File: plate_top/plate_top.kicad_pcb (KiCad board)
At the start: 2 copper layers, 177.4 x 117.9 mm, 32 parts, among them SW1 SW_Push, SW10 SW_Push, SW11 SW_Push, SW12 SW_Push, SW13 SW_Push, SW14 SW_Push, SW15 SW_Push, SW16 SW_Push, SW17 SW_Push, SW18 SW_Push, SW19 SW_Push, SW2 SW_Push, SW20 SW_Push, SW21 SW_Push, SW22 SW_Push, SW23 SW_Push, SW24 SW_Push, SW25 SW_Push, SW26 SW_Push, SW27 SW_Push, SW28 SW_Push, SW29 SW_Push, SW3 SW_Push, SW30 SW_Push, SW31 SW_Push, SW32 SW_Push, SW4 SW_Push, SW5 SW_Push, SW6 SW_Push, SW7 SW_Push, SW8 SW_Push, SW9 SW_Push

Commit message: Plates
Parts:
- added H16: MountingHole, used_footprints:M2_HOLE_PCB, F.Cu at (203.0, 86.6)
- added HM1: CaseHole, used_footprints:M2_HOLE_PCB, F.Cu at (214.5, 114.9)
- added HM10: CaseHole, used_footprints:M2_HOLE_PCB, F.Cu at (171.8, 74.4)
- added HM11: CaseHole, used_footprints:M2_HOLE_PCB, F.Cu at (135.9, 60.3)
- added HM13: CaseHole, used_footprints:M2_HOLE_PCB, F.Cu at (133.3, 105.5)
- added HM14: CaseHole, used_footprints:M2_HOLE_PCB, F.Cu at (176.3, 120.2)
- added HM2: CaseHole, used_footprints:M2_HOLE_PCB, F.Cu at (176.5, 55.3)
- added HM3: CaseHole, used_footprints:M2_HOLE_PCB, F.Cu at (194.2, 134.6)
- added HM4: CaseHole, used_footprints:M2_HOLE_PCB, F.Cu at (155.5, 110.3)
- added HM5: CaseHole, used_footprints:M2_HOLE_PCB, F.Cu at (72.8, 75.9)
- added HM6: CaseHole, used_footprints:M2_HOLE_PCB, F.Cu at (91.4, 80.9)
- added HM7: CaseHole, used_footprints:M2_HOLE_PCB, F.Cu at (96.5, 42.5)
- added HM8: CaseHole, used_footprints:M2_HOLE_PCB, F.Cu at (93.9, 62.0)
- added HM9: CaseHole, used_footprints:M2_HOLE_PCB, F.Cu at (138.5, 44.8)
- moved SW19 51.5 mm to (210.6, 136.5), turned to 127.5 degrees
- moved SW32 33.8 mm to (195.5, 148.1), turned to 307.5 degrees
- moved SW27 30.7 mm to (64.0, 70.0), turned to 172.5 degrees
- moved SW20 30.6 mm to (80.7, 89.1), turned to 172.5 degrees
- moved SW26 30.4 mm to (192.7, 118.2), turned to 141 degrees
- moved SW28 28.6 mm to (122.0, 112.7), turned to 0 degrees
- moved SW21 28.4 mm to (99.6, 91.5), turned to 172.5 degrees
- moved SW31 27.7 mm to (180.8, 133.0), turned to 321 degrees
- moved SW13 27.5 mm to (83.2, 70.2), turned to 172.5 degrees
- moved SW22 25.7 mm to (119.8, 90.2), turned to 168 degrees
- moved SW25 25.1 mm to (175.2, 104.3), turned to 168 degrees
- moved SW14 25.0 mm to (102.1, 72.7), turned to 172.5 degrees
- moved SW7 24.7 mm to (85.7, 51.3), turned to 172.5 degrees
- moved SW29 24.5 mm to (142.8, 114.9), turned to 348 degrees
- moved SW24 24.3 mm to (157.1, 98.1), turned to 168 degrees
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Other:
- board size 177.4 x 117.9 mm -> 170.3 x 138.9 mm

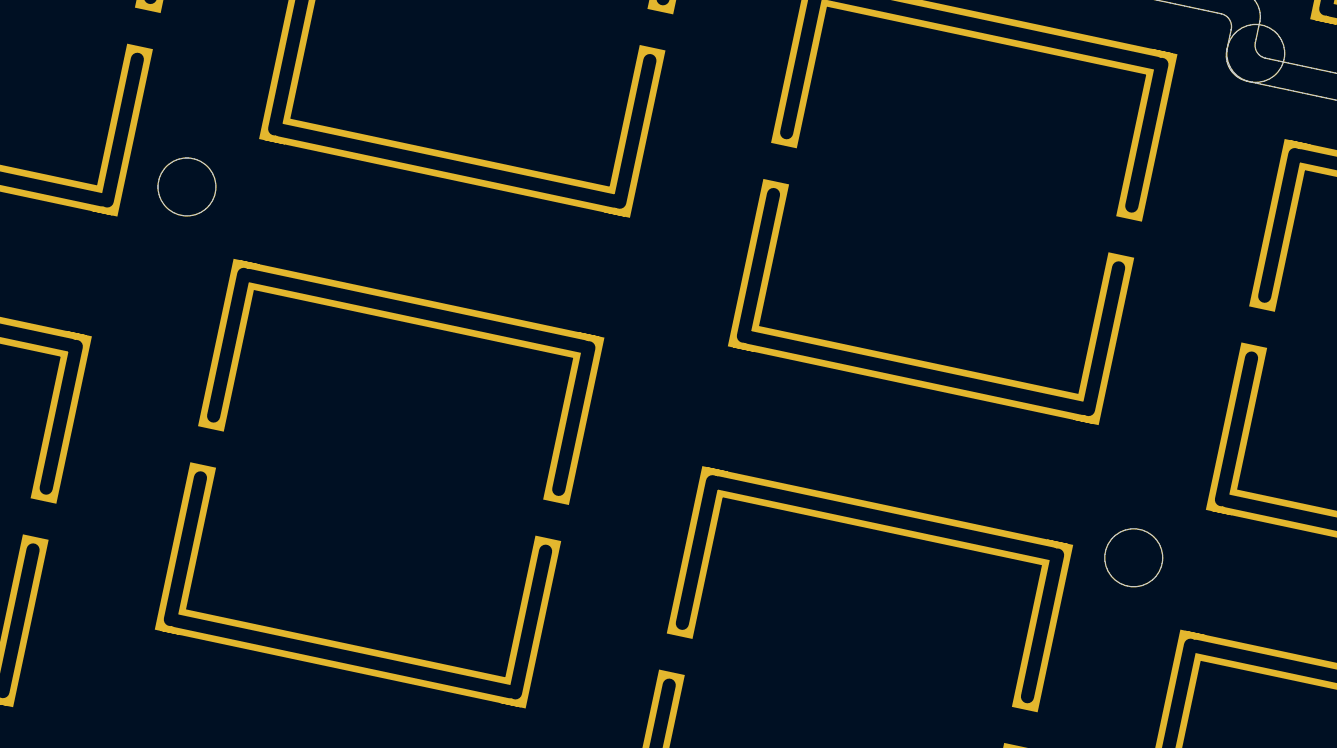
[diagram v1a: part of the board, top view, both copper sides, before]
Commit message: Moved two mounting holes a bit
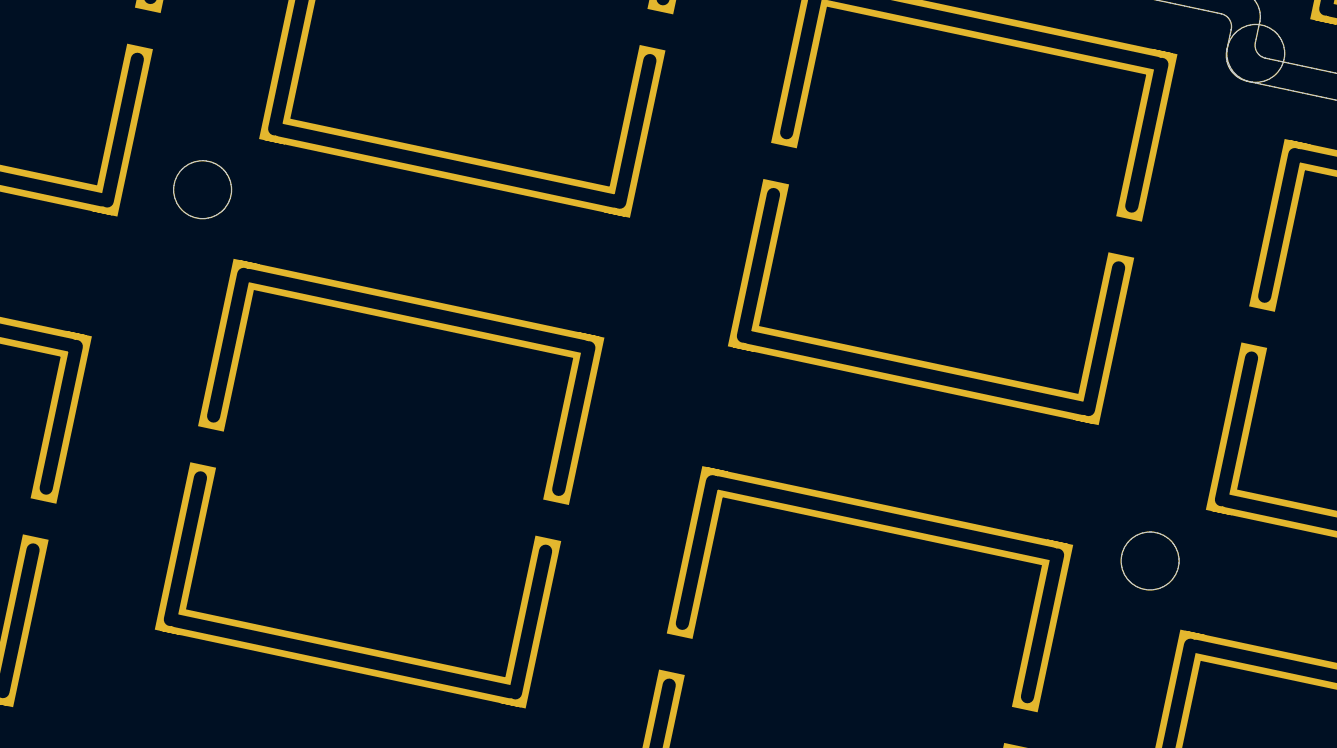
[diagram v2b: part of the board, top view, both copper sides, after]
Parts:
- moved HM10 0.63 mm to (172.5, 74.5)
- moved HM11 0.60 mm to (136.5, 60.4)

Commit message: WIP
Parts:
- moved H16 9.35 mm to (200.2, 95.6)
- moved SW13 9.21 mm to (81.0, 79.1)
- moved SW17 9.21 mm to (158.8, 88.4)
- moved SW20 9.21 mm to (78.5, 98.0)
- moved SW21 9.21 mm to (97.4, 100.5)
- moved SW27 9.21 mm to (61.8, 78.9)
- moved HM14 9.21 mm to (174.1, 129.1)
- moved HM2 9.21 mm to (174.3, 64.2)
- moved HM9 9.21 mm to (136.3, 53.8)
- moved SW10 9.21 mm to (145.0, 61.9)
- moved SW24 9.21 mm to (154.8, 107.0)
- moved SW6 9.21 mm to (184.9, 57.3)
- moved SW7 9.21 mm to (83.5, 60.2)
- moved HM1 9.21 mm to (212.3, 123.8)
- moved HM11 9.21 mm to (134.3, 69.4)
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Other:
- board size 170.3 x 138.9 mm -> 173.5 x 138.9 mm

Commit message: Multiple fixes
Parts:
- moved HM1 12.4 mm to (222.7, 117.2)
- moved HM10 10.9 mm to (172.1, 72.7)
- moved HM11 10.9 mm to (136.2, 58.6)
- moved SW27 10.9 mm to (63.7, 68.2)
- moved HM9 10.9 mm to (138.2, 43.0)
- moved HM8 10.9 mm to (93.6, 60.2)
- moved SW30 10.9 mm to (162.5, 119.9)
- moved SW5 10.9 mm to (168.6, 40.4)
- moved HM2 10.9 mm to (176.2, 53.5)
- moved SW29 10.9 mm to (142.5, 113.1)
- moved SW7 10.9 mm to (85.4, 49.5)
- moved SW24 10.9 mm to (156.7, 96.3)
- moved SW1 10.9 mm to (87.9, 30.6)
- moved SW20 10.9 mm to (80.4, 87.3)
- moved SW14 10.9 mm to (101.8, 70.9)
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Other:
- outline, holes or cut-outs redrawn

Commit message: Holes and top plate
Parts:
- removed H16: MountingHole, used_footprints:M2_HOLE_PCB
- removed HM1: CaseHole, used_footprints:M2_HOLE_PCB
- SW1, SW10, SW11, SW12, SW13, SW14, SW15, SW16, SW17, SW18, SW19, SW2, SW20, SW21, SW22, SW23, SW24, SW25, SW26, SW27, SW28, SW29, SW3, SW30, SW31, SW32, SW4, SW5, SW6, SW7, SW8, SW9: footprint used_footprints:metallized_breakout_cutout -> used_footprints:CherryMX_Hole_for_layout_tester
- moved SW32 23.9 mm to (218.4, 140.8), turned to 319.5 degrees
- moved SW27 23.8 mm to (74.0, 89.6), turned to 183 degrees
- moved HM5 22.7 mm to (83.8, 93.8), turned to 3 degrees
- moved SW20 22.5 mm to (93.9, 105.3), turned to 183 degrees
- moved SW19 22.1 mm to (230.8, 126.3), turned to 139.5 degrees
- moved HM3 21.0 mm to (214.3, 127.9), turned to 4.5 degrees
- moved SW13 20.5 mm to (92.9, 86.3), turned to 183 degrees
- moved SW31 20.5 mm to (200.8, 129.1), turned to 333 degrees
- moved SW28 20.4 mm to (139.2, 121.5), turned to 12 degrees
- moved HM6 20.1 mm to (102.9, 95.3), turned to 3 degrees
- moved SW21 20.0 mm to (113.0, 104.3), turned to 183 degrees
- moved SW7 18.9 mm to (91.9, 67.3), turned to 183 degrees
- moved SW30 18.5 mm to (181.0, 121.8), turned to 346.5 degrees
- moved SW29 18.5 mm to (160.0, 119.3), turned to 0 degrees
- moved HM8 18.1 mm to (101.9, 76.3), turned to 3 degrees
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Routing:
- net (no net): track 0.00 -> 2.48 mm
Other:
- board size 173.5 x 138.9 mm -> 179.4 x 122.5 mm

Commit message: WIP on the top plate
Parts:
- added H15: MountingHole, used_footprints:M2_HOLE_PCB, F.Cu at (224.0, 99.4)
- added HM1: CaseHole, used_footprints:M2_HOLE_PCB, F.Cu at (224.0, 55.0)
- added HM12: CaseHole, used_footprints:M2_HOLE_PCB, F.Cu at (201.0, 87.7)
- moved HM9 7.62 mm to (138.1, 44.9)
- moved HM7 7.47 mm to (98.2, 49.6)
- moved HM2 7.32 mm to (178.3, 46.9)
- moved SW19 7.13 mm to (228.1, 119.7)
- moved SW1 7.13 mm to (88.2, 41.6)
- moved SW22 7.13 mm to (129.6, 93.6)
- moved HM14 7.13 mm to (191.1, 110.9)
- moved HM13 7.13 mm to (146.0, 105.5)
- moved SW21 7.13 mm to (110.3, 97.7)
- moved HM10 7.13 mm to (177.9, 67.0)
- moved SW28 7.13 mm to (136.5, 114.9)
- moved SW32 7.13 mm to (215.7, 134.2)
- moved SW7 7.13 mm to (89.2, 60.7)
- moved SW2 7.13 mm to (107.3, 40.6)
- moved SW17 7.13 mm to (167.7, 74.5)
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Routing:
- net (no net): track 2.48 -> 0.09 mm
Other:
- board size 179.4 x 122.5 mm -> 179.7 x 122.7 mm

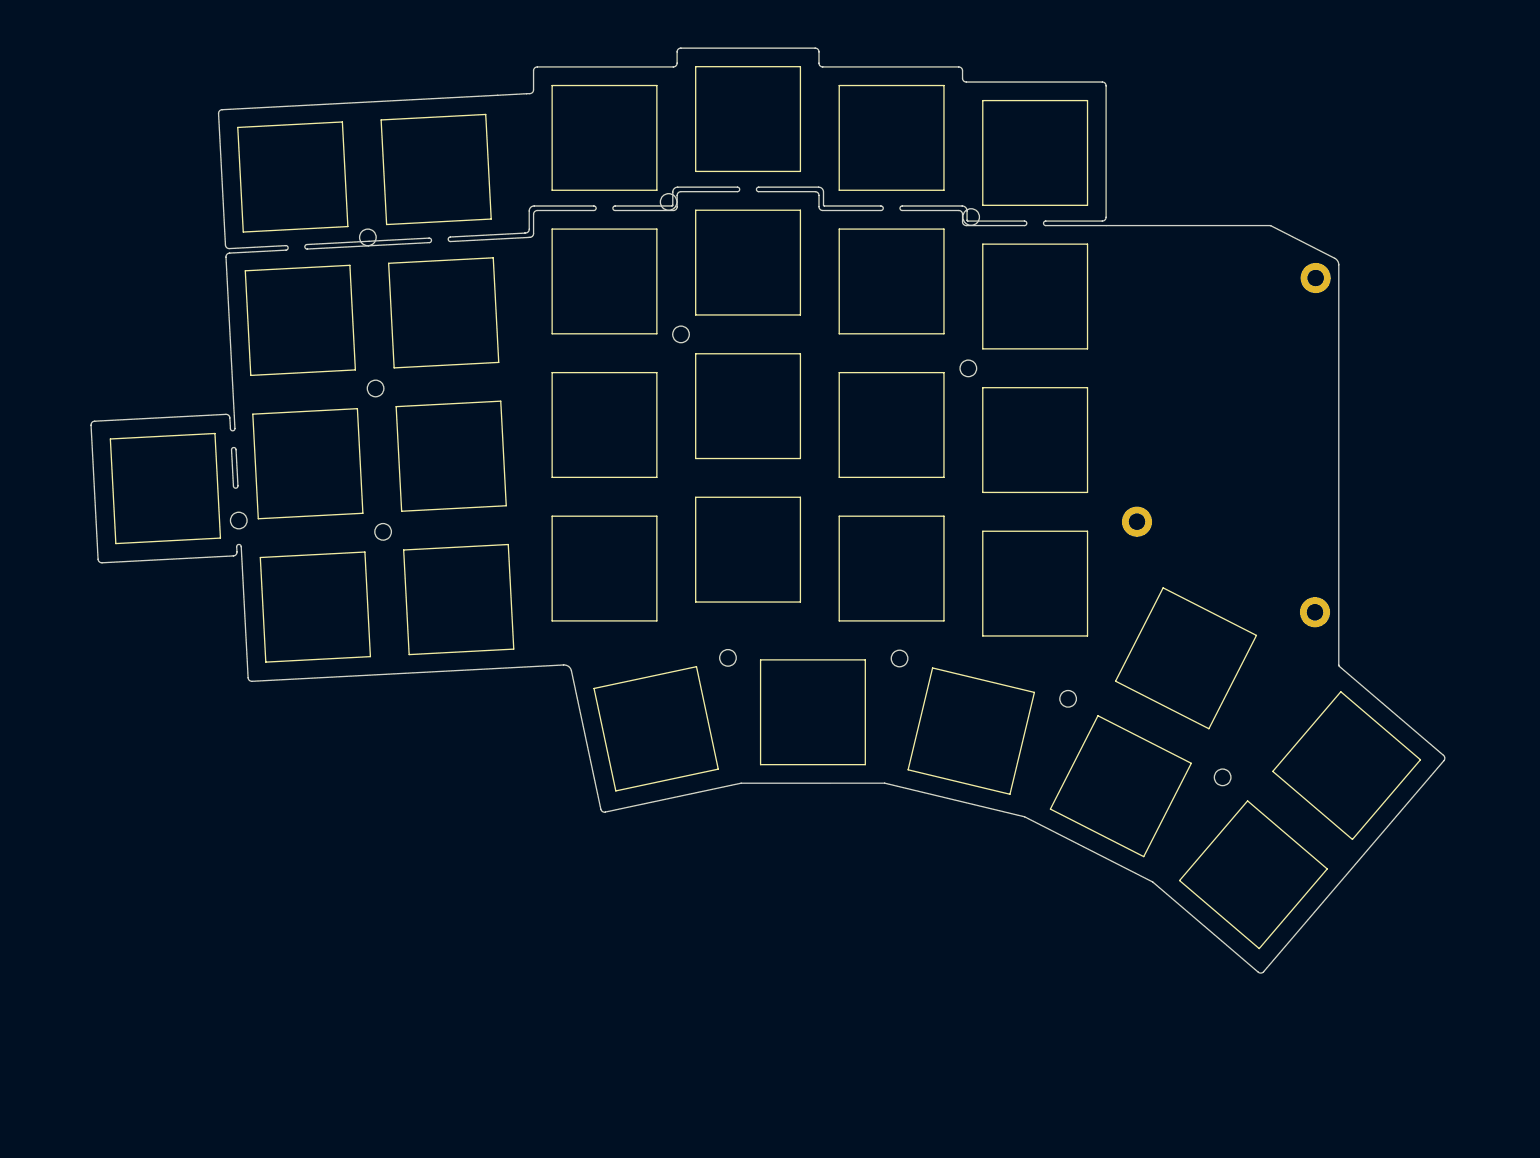
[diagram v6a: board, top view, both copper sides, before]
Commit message: Top plate
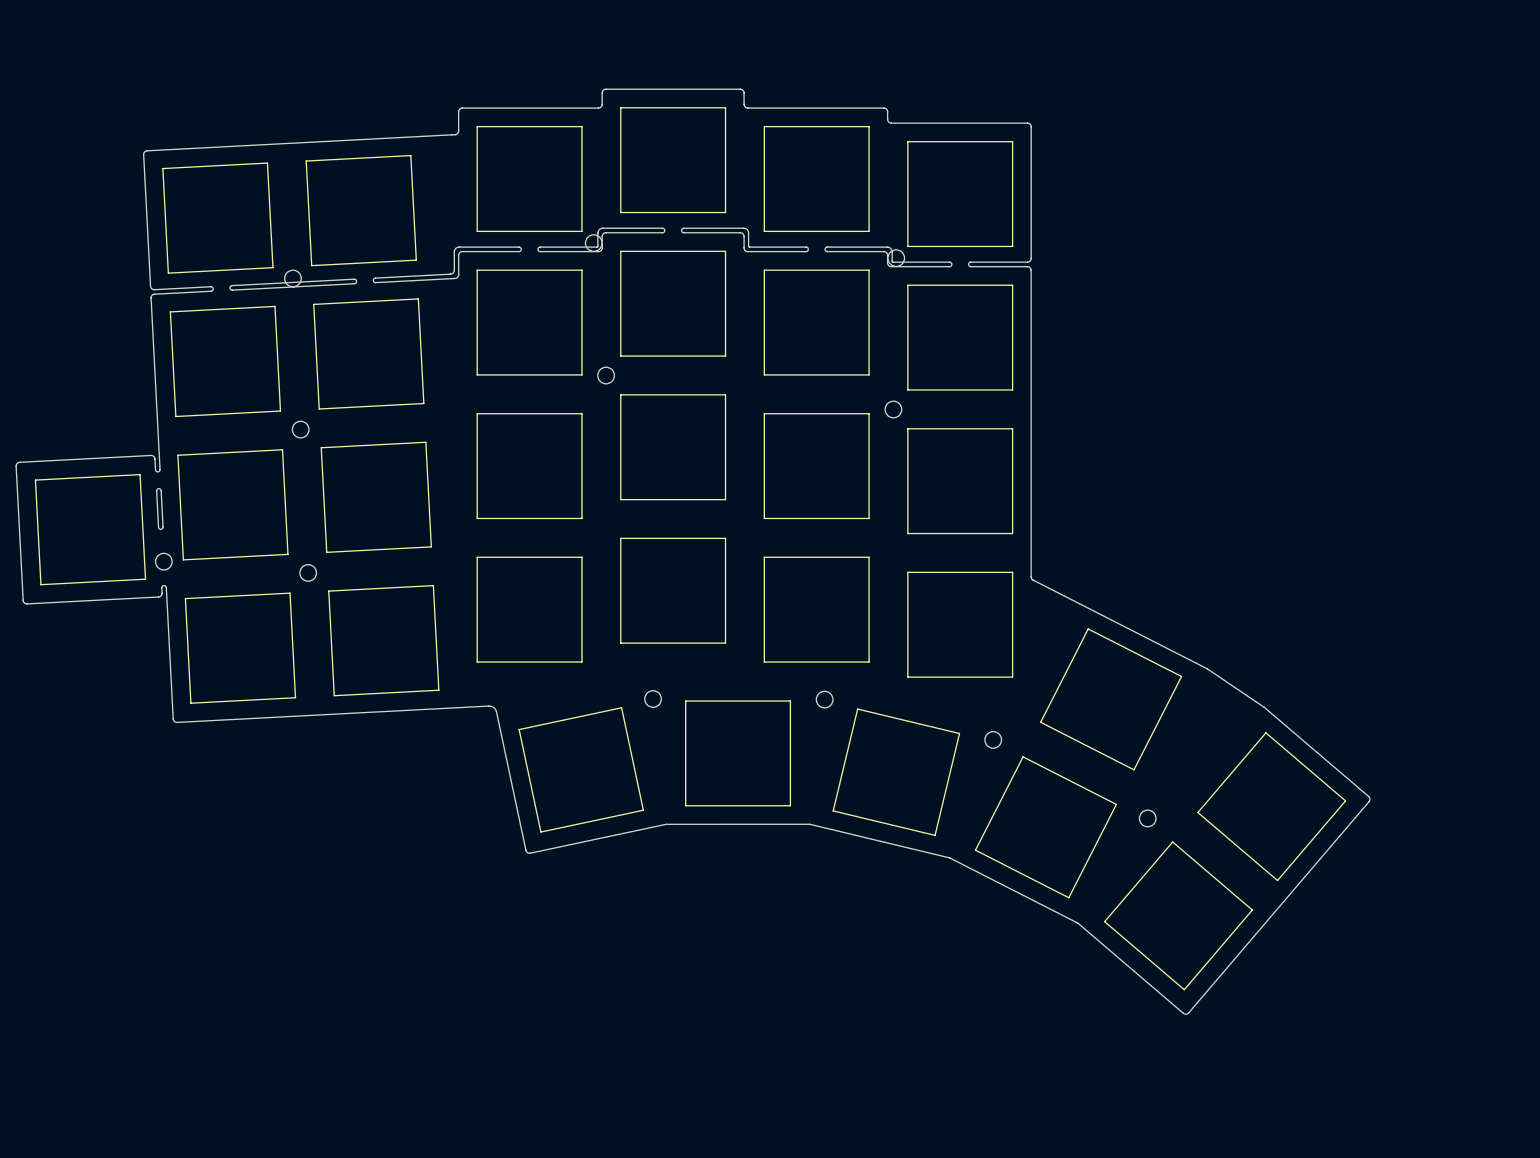
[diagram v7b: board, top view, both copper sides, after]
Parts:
- removed H15: MountingHole, used_footprints:M2_HOLE_PCB
- removed HM1, HM12: CaseHole, used_footprints:M2_HOLE_PCB
- moved SW14 11.3 mm to (99.3, 84.1)
- moved HM14 11.3 mm to (181.2, 116.3)
- moved HM10 11.3 mm to (168.0, 72.5)
- moved SW8 11.3 mm to (98.3, 65.1)
- moved HM7 11.3 mm to (88.3, 55.1)
- moved SW13 11.3 mm to (80.3, 85.1)
- moved SW17 11.3 mm to (157.8, 80.0)
- moved SW3 11.3 mm to (119.7, 41.9)
- moved SW32 11.3 mm to (205.8, 139.7)
- moved SW6 11.3 mm to (176.8, 43.9)
- moved SW2 11.3 mm to (97.3, 46.1)
- moved SW20 11.3 mm to (81.3, 104.2)
- moved SW19 11.3 mm to (218.2, 125.2)
- moved SW25 11.3 mm to (176.8, 101.1)
- moved SW26 11.3 mm to (196.8, 111.0)
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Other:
- outline, holes or cut-outs redrawn

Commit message: Final fixes for v4.1
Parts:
- SW1, SW10, SW11, SW12, SW13, SW14, SW15, SW16, SW17, SW18, SW19, SW2, SW20, SW21, SW22, SW23, SW24, SW25, SW26, SW27, SW28, SW29, SW3, SW30, SW31, SW32, SW4, SW5, SW6, SW7, SW8, SW9: footprint used_footprints:CherryMX_Hole_for_layout_tester -> used_footprints:metallized_breakout_cutout
